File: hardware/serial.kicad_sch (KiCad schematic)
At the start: 9 parts, among them J5 USB_C_Receptacle_USB2.0_14P, U10 CH340C, U5 W65C51NxP, Y2 KC2520Z

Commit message: Fixes and addres fix adding VDA AND VPA
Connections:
- net PHI2 renamed CLK
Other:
- moved on the sheet: J5, R19, R20, R21, R22, R23, U10, U5, Y2

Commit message: Added Bus controller 74HC245
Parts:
- J5: footprint (none) -> Connector_USB:USB_C_Receptacle_Amphenol_12401610E4-2A_CircularHoles
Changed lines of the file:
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@@
 			)
 		)
-		(property "Footprint" ""
+		(property "Footprint" "Connector_USB:USB_C_Receptacle_Amphenol_12401610E4-2A_CircularHoles"
 			(at 205.74 90.17 0)
 			(effects

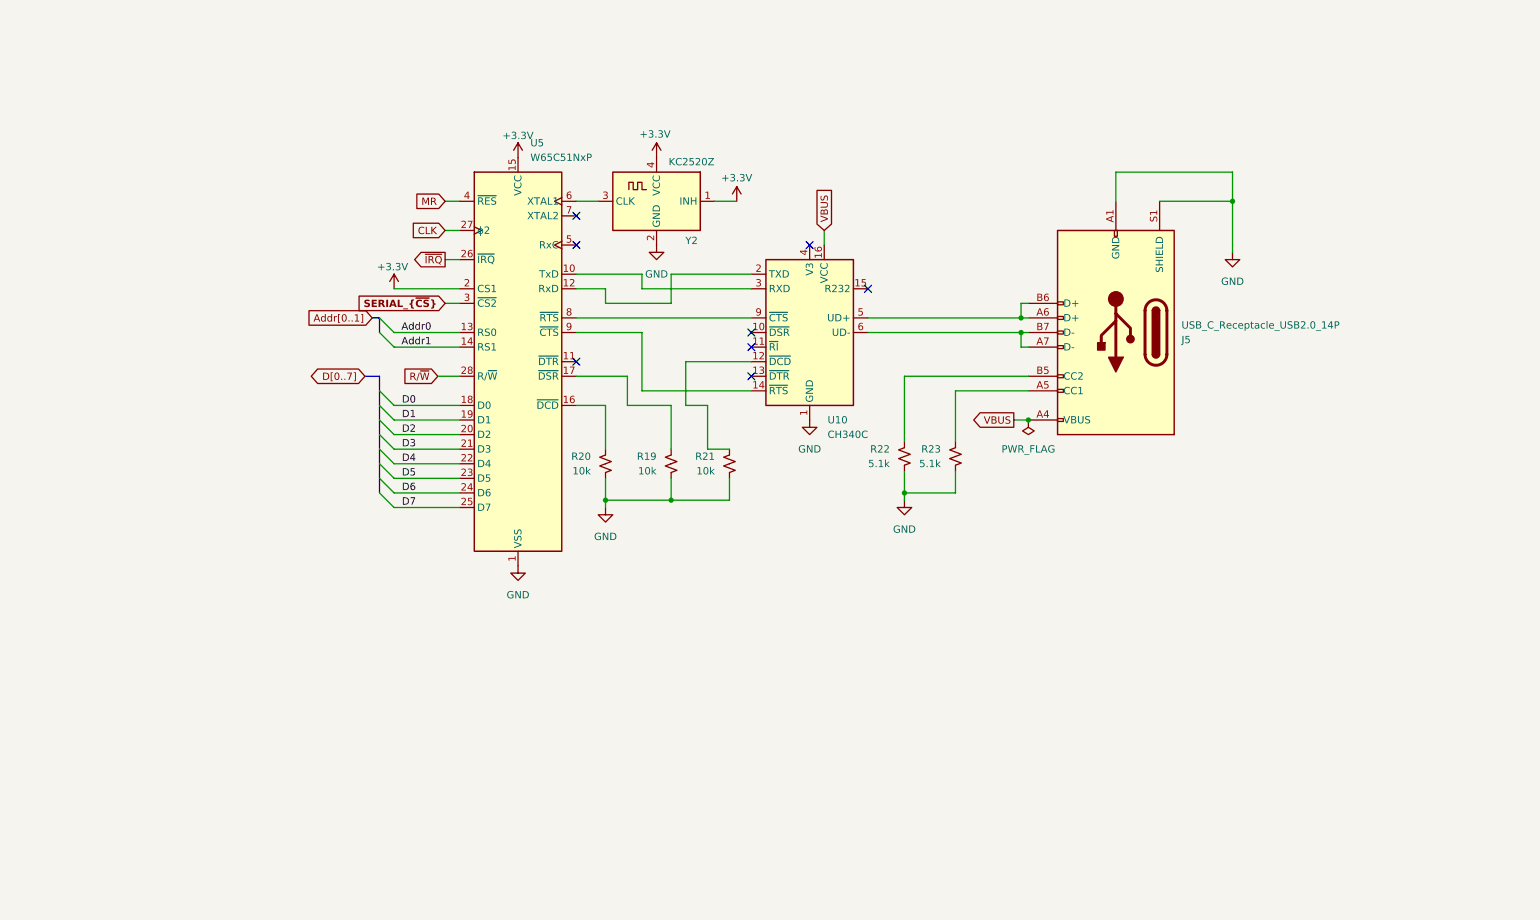
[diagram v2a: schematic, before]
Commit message: IMproved Serial With New CHIP, IMproved Video, Added external Serial Connections
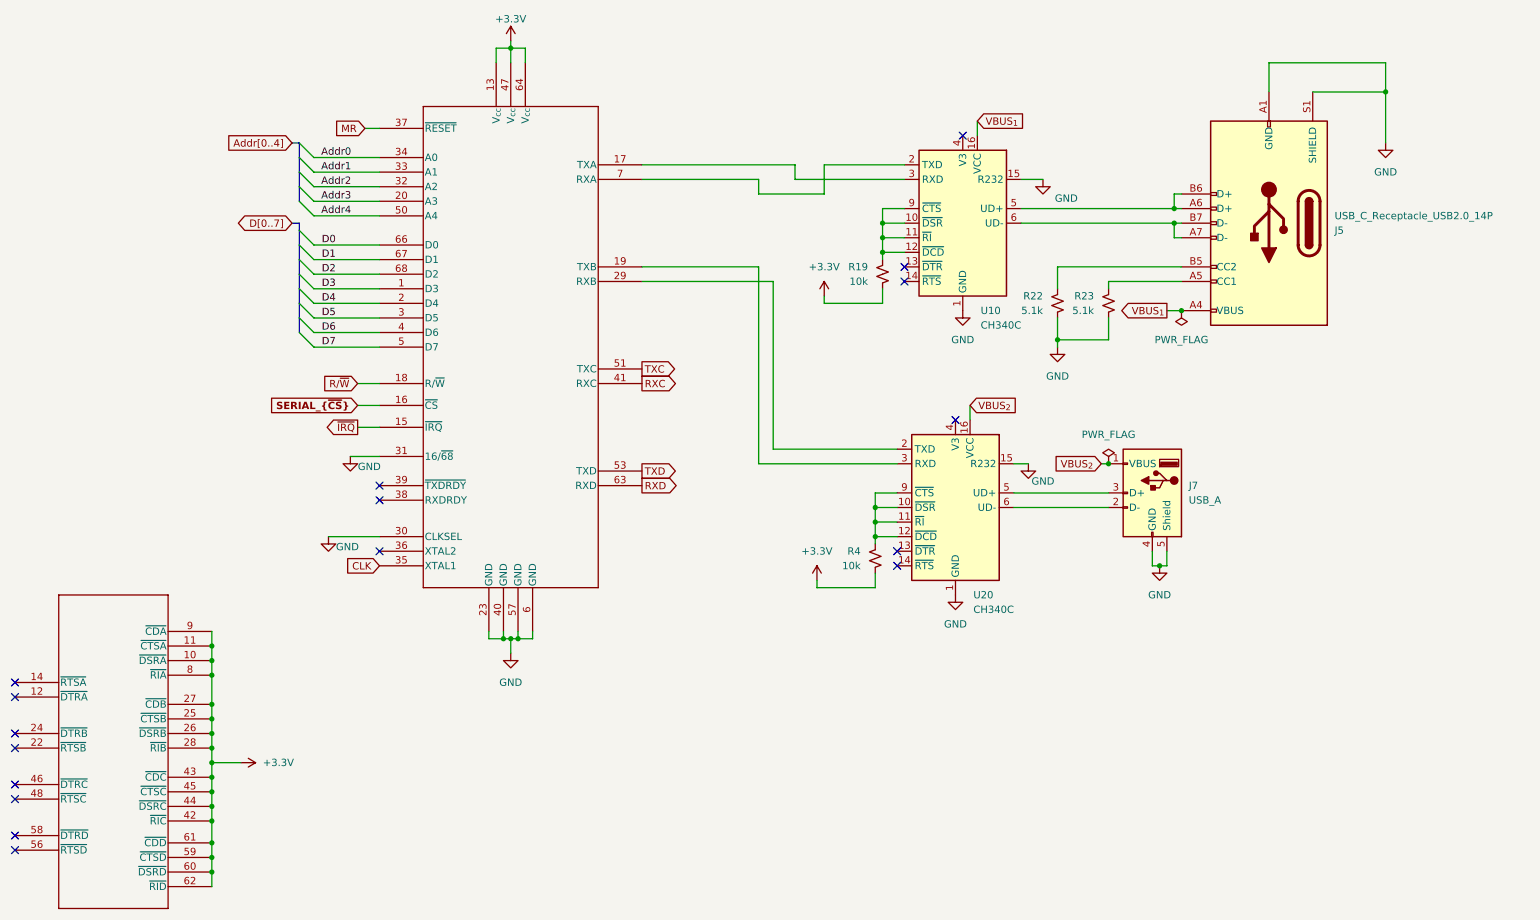
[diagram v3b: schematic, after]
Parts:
- removed R20, R21: 10k, Resistor_SMD:R_0603_1608Metric, symbol Device:R_Small_US
- removed U5: W65C51NxP, Package_DIP:DIP-28_W15.24mm, symbol 65xx-library:W65C51NxP
- removed Y2: KC2520Z, Oscillator:Oscillator_SMD_Kyocera_KC2520Z-4Pin_2.5x2.0mm, symbol Oscillator:KC2520Z
- added J7: USB_A, symbol Connector:USB_A
- added R4: 10k, Resistor_SMD:R_0603_1608Metric, symbol Device:R_Small_US
- added U20: CH340C, Package_SO:SOIC-16_3.9x9.9mm_P1.27mm, symbol Interface_USB:CH340C
- added U5: SC16C654DBIB64_151, Package_QFP:LQFP-64_7x7mm_P0.4mm, symbol 2026-07-13_16-03-59:SC16C654DBIB64_151
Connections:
- net +3.3V: now also R19.2, R4.2, U5.10 (~{DSRA}), U5.11 (~{CTSA}), U5.13 (V_{cc}), U5.25 (~{CTSB}), U5.26 (~{DSRB}), U5.27 (~{CDB}), U5.28 (~{RIB}), U5.42 (~{RIC}), U5.43 (~{CDC}), U5.44 (~{DSRC}), U5.45 (~{CTSC}), U5.47 (V_{cc}), U5.59 (~{CTSD}), U5.60 (~{DSRD}), U5.61 (~{CDD}), U5.62 (~{RID}), U5.64 (V_{cc}), U5.8 (~{RIA}), U5.9 (~{CDA})
- net Addr0: now also U5.34 (A0)
- net Addr1: now also U5.33 (A1)
- net CLK: now also U5.35 (XTAL1)
- net D0: now also U5.66 (D0)
- net D1: now also U5.67 (D1)
- net D2: now also U5.68 (D2)
- net D3: now also U5.1 (D3)
- net D4: now also U5.2 (D4)
- net D5: now also U5.3 (D5)
- net D6: now also U5.4 (D6)
- net D7: now also U5.5 (D7)
- net GND: now also U10.15 (R232), J7.4 (GND), J7.5 (Shield), U20.1 (GND), U20.15 (R232), U5.23 (GND), U5.30 (CLKSEL), U5.31 (16/~{68}), U5.40 (GND), U5.57 (GND), U5.6 (GND); no longer R19.2
- net MR: now also U5.37 (~{RESET})
- net R/~{W}: now also U5.18 (R/~{W})
- net SERIAL_{~{CS}}: now also U5.16 (~{CS})
- net ~{IRQ}: now also U5.15 (~{IRQ})
- net at U10.10 (~{DSR}): now also R19.1, U10.11 (~{RI}), U10.12 (~{DCD}), U10.9 (~{CTS})
- net at U10.2 (TXD): now also U5.7 (RXA)
- net at U10.3 (RXD): now also U5.17 (TXA)
- net VBUS renamed VBUS_{1}
- new net: U20.3 (RXD), U5.19 (TXB)
- new net: U20.2 (TXD), U5.29 (RXB)
- new net: R4.1, U20.10 (~{DSR}), U20.11 (~{RI}), U20.12 (~{DCD}), U20.9 (~{CTS})
- new net: J7.3 (D+), U20.5 (UD+)
- new net: J7.2 (D-), U20.6 (UD-)
- new net Addr2: U5.32 (A2)
- new net Addr3: U5.20 (A3)
- new net Addr4: U5.50 (A4)
- new net RXC: U5.41 (RXC)
- new net RXD: U5.63 (RXD)
- new net TXC: U5.51 (TXC)
- new net TXD: U5.53 (TXD)
- new net VBUS_{2}: J7.1 (VBUS), U20.16 (VCC)
- no-connect marks 8 -> 17
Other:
- title: (none) -> Lambda One - Serial Communication
- moved on the sheet: J5, R19, R22, R23, U10
